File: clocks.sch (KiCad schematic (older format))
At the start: 10 parts, among them U11 5M1270ZT144C5N, U14 Si5351A-B-GT, X1 CB3LV-3I-100M0000, Y1 25MHZ 8PF

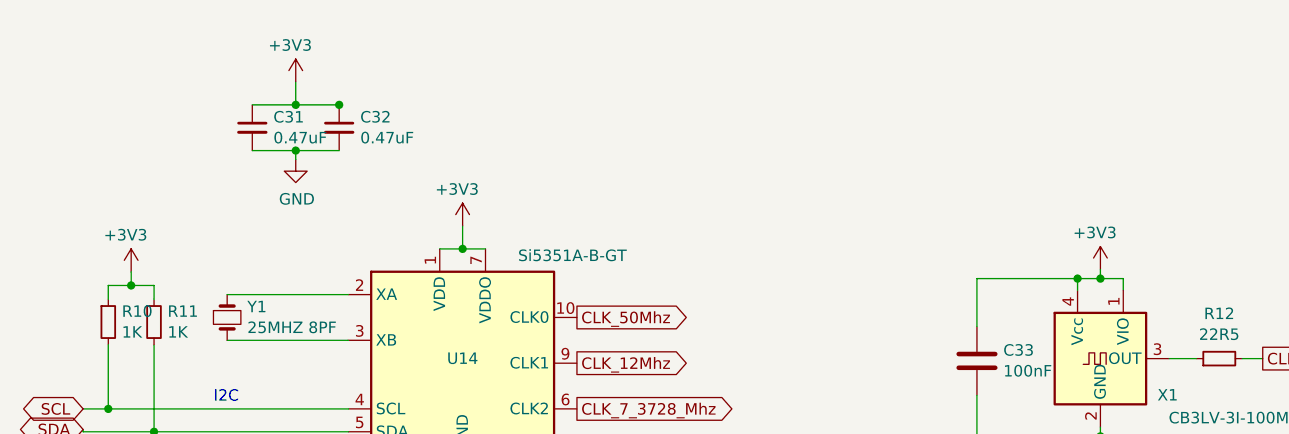
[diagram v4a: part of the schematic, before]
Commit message: consolidated power supply
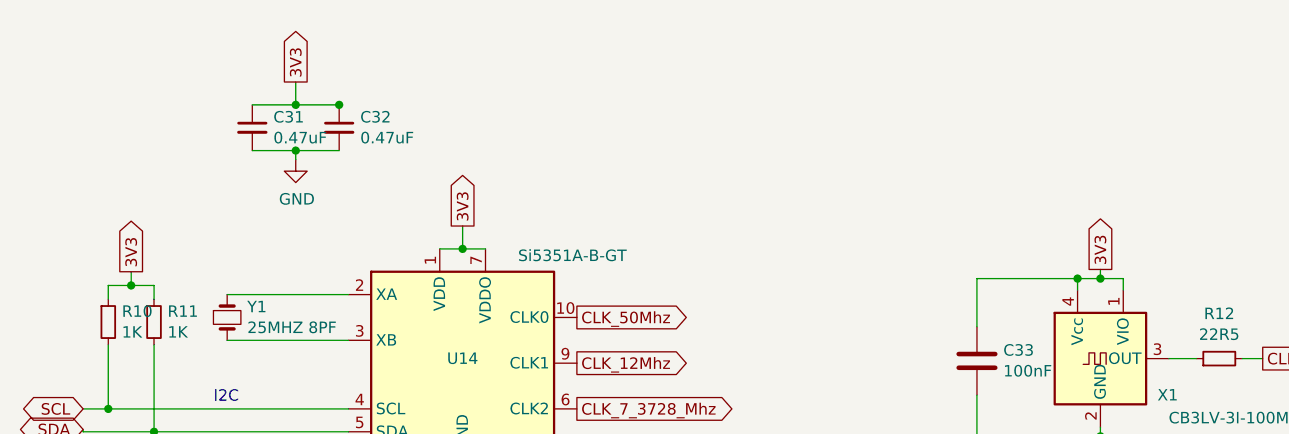
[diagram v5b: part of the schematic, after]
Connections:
- net labels added: 3V3
- net labels removed: +3V3
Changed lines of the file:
@@
-	1    0    0    -1
-$EndComp
-$Comp
-L power:+3V3 #PWR?
-U 1 1 5D0055A7
-P 5530 1730
-AR Path="/5D0055A7" Ref="#PWR?"  Part="1"
-AR Path="/5D0F9837/5D0055A7" Ref="#PWR?"  Part="1"
-AR Path="/5CFABACD/5D0055A7" Ref="#PWR?"  Part="1"
-AR Path="/5CFABACD/5CFFC458/5D0055A7" Ref="#PWR063"  Part="1"
-F 0 "#PWR063" H 5530 1580 50  0001 C CNN
-F 1 "+3V3" H 5410 1890 50  0000 L CNN
-F 2 "" H 5530 1730 50  0001 C CNN
-F 3 "" H 5530 1730 50  0001 C CNN
-	1    5530 1730
 	1    0    0    -1
 $EndComp
@@
 	2740 1640 2840 1640
 $Comp
-L power:+3V3 #PWR?
-U 1 1 5D00B94C
-P 2740 1540
-AR Path="/5D00B94C" Ref="#PWR?"  Part="1"
-AR Path="/5D0F9837/5D00B94C" Ref="#PWR?"  Part="1"
-AR Path="/5CFABACD/5D00B94C" Ref="#PWR?"  Part="1"
-AR Path="/5CFABACD/5CFFC458/5D00B94C" Ref="#PWR062"  Part="1"
-F 0 "#PWR062" H 2740 1390 50  0001 C CNN
-F 1 "+3V3" H 2620 1700 50  0000 L CNN
-F 2 "" H 2740 1540 50  0001 C CNN
-F 3 "" H 2740 1540 50  0001 C CNN
-	1    2740 1540
-	1    0    0    -1
-$EndComp
-$Comp
 L Device:C_Small C31
 U 1 1 5D00C0F7
@@
 Wire Wire Line
 	2010 1010 2010 910
-$Comp
-L power:+3V3 #PWR?
-U 1 1 5D00F92A
-P 2010 910
-AR Path="/5D00F92A" Ref="#PWR?"  Part="1"
-AR Path="/5D0F9837/5D00F92A" Ref="#PWR?"  Part="1"
-AR Path="/5CFABACD/5D00F92A" Ref="#PWR?"  Part="1"
-AR Path="/5CFABACD/5CFFC458/5D00F92A" Ref="#PWR060"  Part="1"
-F 0 "#PWR060" H 2010 760 50  0001 C CNN
-F 1 "+3V3" H 1890 1070 50  0000 L CNN
-F 2 "" H 2010 910 50  0001 C CNN
-F 3 "" H 2010 910 50  0001 C CNN
-	1    2010 910
-	1    0    0    -1
-$EndComp
 Connection ~ 2010 1010
 Wire Wire Line
@@
 Wire Wire Line
 	1290 1800 1390 1800
-$Comp
-L power:+3V3 #PWR?
-U 1 1 5D01ACA8
-P 1290 1740
-AR Path="/5D01ACA8" Ref="#PWR?"  Part="1"
-AR Path="/5D0F9837/5D01ACA8" Ref="#PWR?"  Part="1"
-AR Path="/5CFABACD/5D01ACA8" Ref="#PWR?"  Part="1"
-AR Path="/5CFABACD/5CFFC458/5D01ACA8" Ref="#PWR064"  Part="1"
-F 0 "#PWR064" H 1290 1590 50  0001 C CNN
-F 1 "+3V3" H 1170 1900 50  0000 L CNN
-F 2 "" H 1290 1740 50  0001 C CNN
-F 3 "" H 1290 1740 50  0001 C CNN
-	1    1290 1740
-	1    0    0    -1
-$EndComp
 Text GLabel 4020 3670 0    50   Input ~ 0
 CLK_7_3728_Mhz
@@
 Text Notes 1650 2320 0    50   ~ 0
 I2C
+Text GLabel 5530 1730 1    50   Output ~ 0
+3V3
+Text GLabel 2740 1540 1    50   Output ~ 0
+3V3
+Text GLabel 2010 910  1    50   Output ~ 0
+3V3
+Text GLabel 1290 1740 1    50   Output ~ 0
+3V3
 $EndSCHEMATC

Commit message: Updated BOM
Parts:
- C31, C32: MFR (none) -> Taiyo Yuden; MPN (none) -> JMK107B7474KA-T; SPR (none) -> Mouser
- C33: MFR KEMET -> Taiyo Yuden; MPN C0805C104K4RACTU -> TMK107BJ104KA-T; SPN 80-C0805C104K4R -> (none)
- R10, R11: MFR (none) -> Yageo; MPN (none) -> RC0603JR-071KL; SPR (none) -> Mouser
- R12: MFR (none) -> Yageo; MPN (none) -> RC0603JR-0722RL; SPR (none) -> Mouser
- U11: MFR (none) -> Intel; MPN (none) -> 5M1270ZT144C5N; Manufacturer_Name Intel -> (none); SPR (none) -> Mouser
- U14: MFR (none) -> Silicon Laboratories; MPN (none) -> SI5351A-B-GT; SPR (none) -> Mouser
- X1: MFR (none) -> CTI; MPN (none) -> CB3LV-3I-100M0000; SPR (none) -> Mouser
- Y1: MFR (none) -> NDK; MPN (none) -> NX5032GA-25.000M-LN-CD-1; SPR (none) -> Mouser
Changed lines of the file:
@@
 F 2 "Oscillator:Oscillator_SMD_SeikoEpson_SG8002CA-4Pin_7.0x5.0mm_HandSoldering" H 5530 1770 50  0001 C CNN
 F 3 "https://www.mouser.com/datasheet/2/96/008-0256-0-786323.pdf" H 5430 2120 50  0001 C CNN
+F 4 "CTI" H 5530 2120 50  0001 C CNN "MFR"
+F 5 "CB3LV-3I-100M0000" H 5530 2120 50  0001 C CNN "MPN"
+F 6 "Mouser" H 5530 2120 50  0001 C CNN "SPR"
 	1    5530 2120
 	1    0    0    -1
@@
 F 2 "Resistor_SMD:R_0603_1608Metric_Pad1.05x0.95mm_HandSolder" H 6050 2120 50  0001 C CNN
 F 3 "~" H 6050 2120 50  0001 C CNN
+F 4 "Yageo" H 6050 2120 50  0001 C CNN "MFR"
+F 5 "RC0603JR-0722RL" H 6050 2120 50  0001 C CNN "MPN"
+F 6 "Mouser" H 6050 2120 50  0001 C CNN "SPR"
 	1    6050 2120
 	0    -1   -1   0
@@
 F 2 "Capacitor_SMD:C_0603_1608Metric_Pad1.05x0.95mm_HandSolder" H 5028 1980 50  0001 C CNN
 F 3 "https://www.mouser.com/datasheet/2/212/KEM_C1002_X7R_SMD-1102033.pdf" H 4990 2130 50  0001 C CNN
-F 4 "KEMET" H -310 -4570 50  0001 C CNN "MFR"
-F 5 "C0805C104K4RACTU" H -310 -4570 50  0001 C CNN "MPN"
+F 4 "Taiyo Yuden" H -310 -4570 50  0001 C CNN "MFR"
+F 5 "TMK107BJ104KA-T" H -310 -4570 50  0001 C CNN "MPN"
 F 6 "Mouser" H -310 -4570 50  0001 C CNN "SPR"
-F 7 "80-C0805C104K4R" H -310 -4570 50  0001 C CNN "SPN"
-F 8 "https://www.mouser.com/ProductDetail/KEMET/C0805C104K4RACTU?qs=sGAEpiMZZMs0AnBnWHyRQFCCI5cSbRT%2F1Gdrl2EbPVM%3D" H -310 -4570 50  0001 C CNN "SPURL"
+F 7 "https://www.mouser.com/ProductDetail/KEMET/C0805C104K4RACTU?qs=sGAEpiMZZMs0AnBnWHyRQFCCI5cSbRT%2F1Gdrl2EbPVM%3D" H -310 -4570 50  0001 C CNN "SPURL"
 	1    4990 2130
 	1    0    0    -1
@@
 F 4 "CPLD - Complex Programmable Logic Devices CPLD - MAX V 980 Macro 114 IOs" H 6420 6270 50  0001 L CNN "Description"
 F 5 "1.55" H 6420 6170 50  0001 L CNN "Height"
-F 6 "Intel" H 6420 5870 50  0001 L CNN "Manufacturer_Name"
-F 7 "5M1270ZT144C5N" H 6420 5770 50  0001 L CNN "Manufacturer_Part_Number"
+F 6 "5M1270ZT144C5N" H 6420 5770 50  0001 L CNN "Manufacturer_Part_Number"
+F 7 "Intel" H 4580 3570 50  0001 C CNN "MFR"
+F 8 "5M1270ZT144C5N" H 4580 3570 50  0001 C CNN "MPN"
+F 9 "Mouser" H 4580 3570 50  0001 C CNN "SPR"
 	5    4580 3570
 	1    0    0    -1
@@
 F 2 "Package_SO:MSOP-10_3x3mm_P0.5mm" H 2740 1340 50  0001 C CNN
 F 3 "https://www.silabs.com/documents/public/data-sheets/Si5351-B.pdf" H 2390 2040 50  0001 C CNN
+F 4 "Silicon Laboratories" H 2740 2140 50  0001 C CNN "MFR"
+F 5 "SI5351A-B-GT" H 2740 2140 50  0001 C CNN "MPN"
+F 6 "Mouser" H 2740 2140 50  0001 C CNN "SPR"
 	1    2740 2140
 	1    0    0    -1
@@
 F 2 "Crystal:Crystal_SMD_TXC_7A-2Pin_5x3.2mm" H 1710 1940 50  0001 C CNN
 F 3 "https://www.mouser.com/datasheet/2/905/ndk_04232018_NX5032GA-LN-CD-1-1324922.pdf" H 1710 1940 50  0001 C CNN
+F 4 "Mouser" H 1710 1940 50  0001 C CNN "SPR"
+F 5 "NDK" H 1710 1940 50  0001 C CNN "MFR"
+F 6 "NX5032GA-25.000M-LN-CD-1" H 1710 1940 50  0001 C CNN "MPN"
 	1    1710 1940
 	0    1    1    0
@@
 F 2 "Capacitor_SMD:C_0603_1608Metric_Pad1.05x0.95mm_HandSolder" H 1820 1110 50  0001 C CNN
 F 3 "~" H 1820 1110 50  0001 C CNN
+F 4 "Taiyo Yuden" H 1820 1110 50  0001 C CNN "MFR"
+F 5 "JMK107B7474KA-T" H 1820 1110 50  0001 C CNN "MPN"
+F 6 "Mouser" H 1820 1110 50  0001 C CNN "SPR"
 	1    1820 1110
 	1    0    0    -1
@@
 F 2 "Capacitor_SMD:C_0603_1608Metric_Pad1.05x0.95mm_HandSolder" H 2200 1110 50  0001 C CNN
 F 3 "~" H 2200 1110 50  0001 C CNN
+F 4 "Taiyo Yuden" H 2200 1110 50  0001 C CNN "MFR"
+F 5 "JMK107B7474KA-T" H 2200 1110 50  0001 C CNN "MPN"
+F 6 "Mouser" H 2200 1110 50  0001 C CNN "SPR"
 	1    2200 1110
 	1    0    0    -1
@@
 F 2 "Resistor_SMD:R_0603_1608Metric_Pad1.05x0.95mm_HandSolder" H 1190 1960 50  0001 C CNN
 F 3 "~" H 1190 1960 50  0001 C CNN
+F 4 "Yageo" H 1190 1960 50  0001 C CNN "MFR"
+F 5 "RC0603JR-071KL" H 1190 1960 50  0001 C CNN "MPN"
+F 6 "Mouser" H 1190 1960 50  0001 C CNN "SPR"
 	1    1190 1960
 	1    0    0    -1
@@
 F 2 "Resistor_SMD:R_0603_1608Metric_Pad1.05x0.95mm_HandSolder" H 1390 1960 50  0001 C CNN
 F 3 "~" H 1390 1960 50  0001 C CNN
+F 4 "Yageo" H 1390 1960 50  0001 C CNN "MFR"
+F 5 "RC0603JR-071KL" H 1390 1960 50  0001 C CNN "MPN"
+F 6 "Mouser" H 1390 1960 50  0001 C CNN "SPR"
 	1    1390 1960
 	1    0    0    -1

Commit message: updated descriptions and part #'s
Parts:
- C31, C32: Description (none) -> Multilayer Ceramic Capacitors MLCC - SMD/SMT 0603 6.3V 0.47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; SPN (none) -> 963-JMK107B7474KA-T; SPURL (none) -> https://www.mouser.com/ProductDetail/963-JMK107B7474KA-T
- C33: Description (none) -> Multilayer Ceramic Capacitors MLCC - SMD/SMT 0.1uF 25V X5R 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; SPN (none) -> 963-TMK107BJ104KA-T; SPURL https://www.mouser.com/ProductDetail/KEMET/C0805C104K4RACTU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 -> https://www.mouser.com/ProductDetail/963-TMK107BJ104KA-T
- R10, R11: Description (none) -> Thick Film Resistors - SMD 1K OHM 5%; SPN (none) -> 603-RC0603JR-071KL; SPURL (none) -> https://www.mouser.com/ProductDetail/603-RC0603JR-071KL
- R12: Description (none) -> Thick Film Resistors - SMD 22 OHM 5%; SPN (none) -> 603-RC0603JR-0722RL; SPURL (none) -> https://www.mouser.com/ProductDetail/603-RC0603JR-0722RL
- U11: SPN (none) -> 989-5M1270ZT144C5N; SPURL (none) -> https://www.mouser.com/ProductDetail/989-5M1270ZT144C5N
- U14: Description (none) -> Clock Generators & Support Products I2C program, any-freque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; SPN (none) -> 634-SI5351A-B-GT; SPURL (none) -> https://www.mouser.com/ProductDetail/634-SI5351A-B-GT
- X1: Description (none) -> Standard Clock Oscillators 100.0MHz 3.3V -40C +85C; SPN (none) -> 774-CB3LV-3I-100M0; SPURL (none) -> https://www.mouser.com/ProductDetail/774-CB3LV-3I-100M0
- Y1: Description (none) -> Crystals CRYSTAL 25MHZ 8PF SMD; SPN (none) -> 344-NX5032GA25MLNCD1; SPURL (none) -> https://www.mouser.com/ProductDetail/344-NX5032GA25MLNCD1

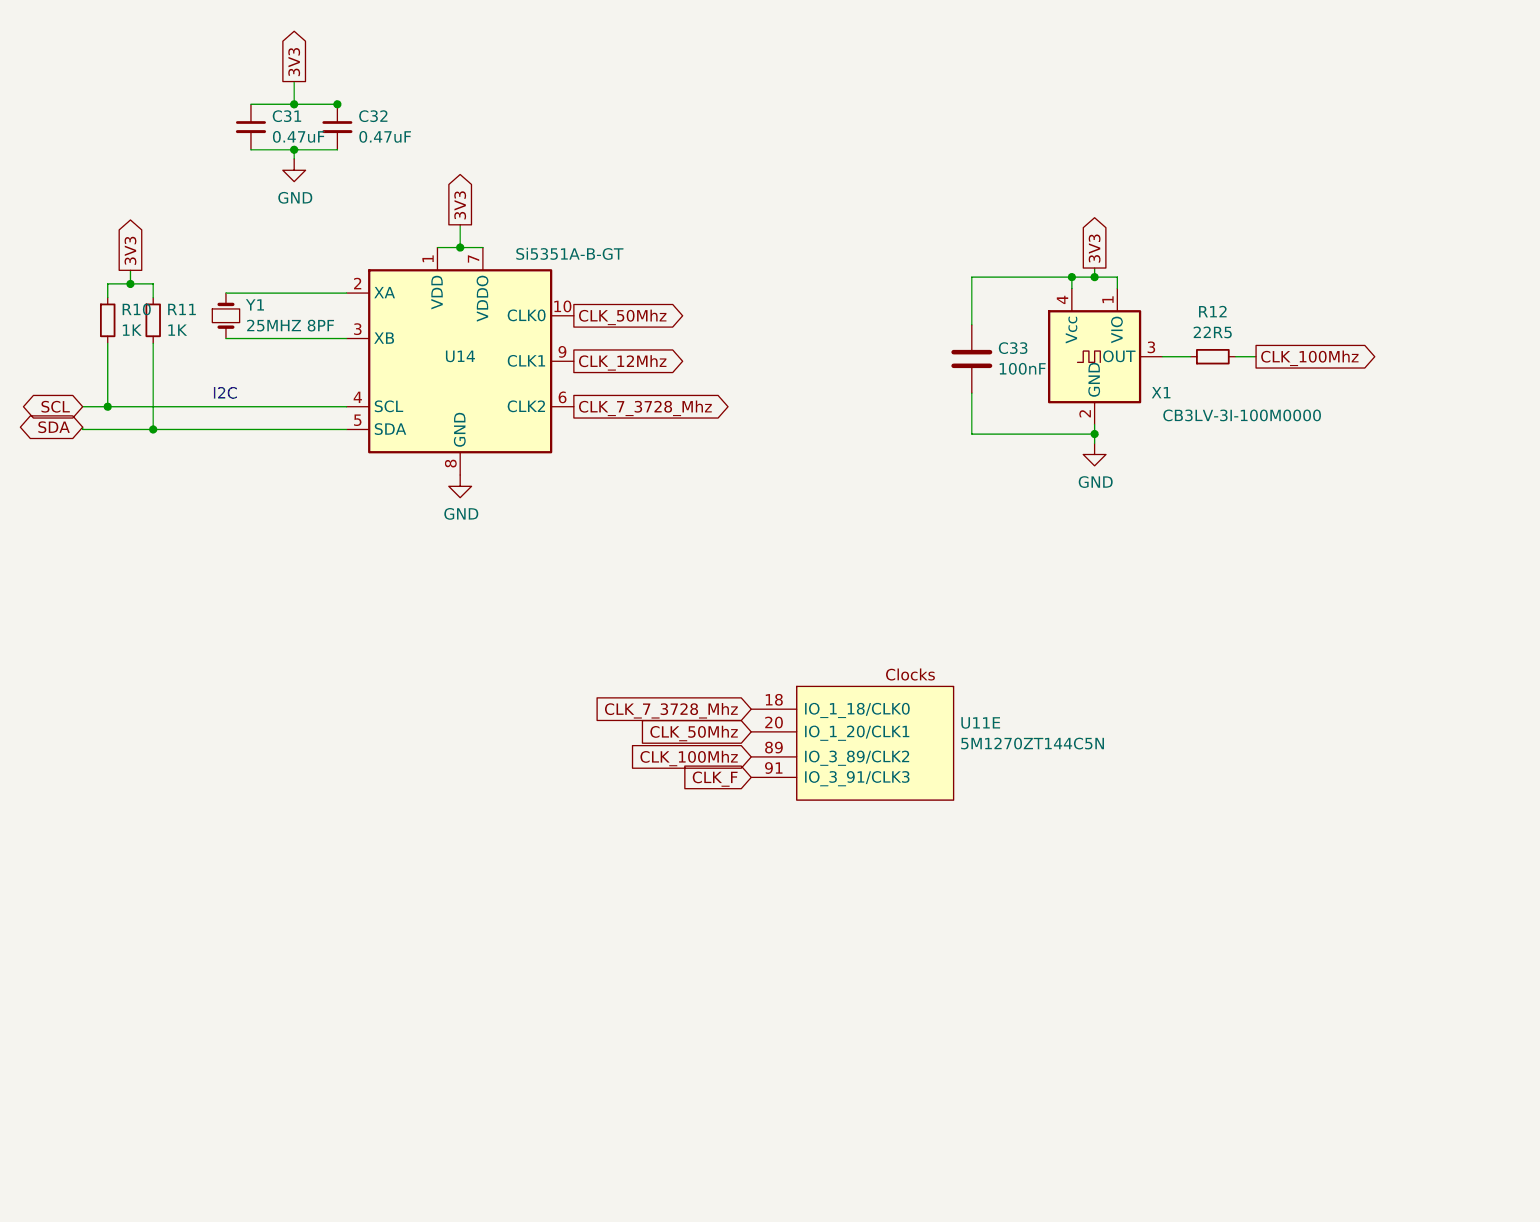
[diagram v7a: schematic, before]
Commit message: added clock controller/programmer
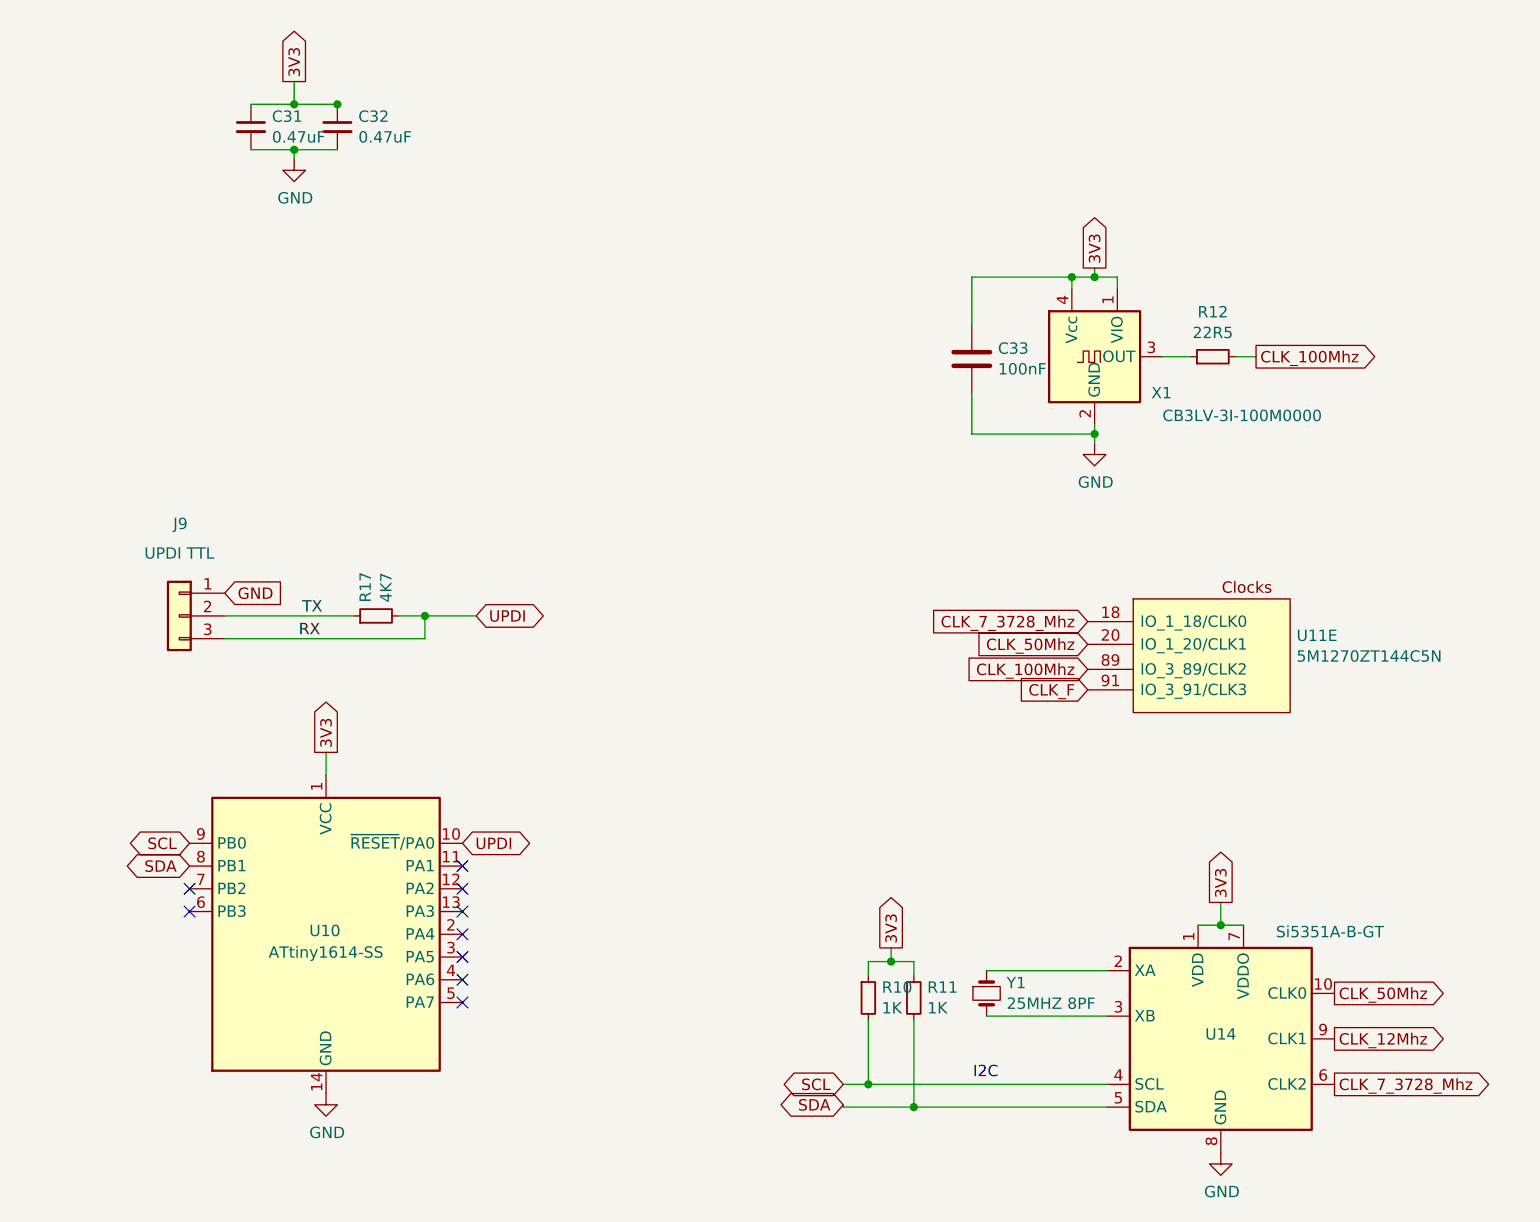
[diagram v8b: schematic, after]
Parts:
- added J9: UPDI TTL, Connector_PinHeader_2.54mm:PinHeader_1x03_P2.54mm_Horizontal, symbol Connector_Generic:Conn_01x03
- added R17: 4K7, Resistor_SMD:R_0603_1608Metric_Pad1.05x0.95mm_HandSolder, symbol Device:R_Small
- added U10: ATtiny1614-SS, Package_SO:SOIC-14_3.9x8.7mm_P1.27mm, symbol MCU_Microchip_ATtiny:ATtiny1614-SS
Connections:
- net labels added: RX, TX, UPDI
- wire segments 37 -> 43
- no-connect marks 0 -> 9
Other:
- moved on the sheet: R10, R11, U11E, U14, Y1
